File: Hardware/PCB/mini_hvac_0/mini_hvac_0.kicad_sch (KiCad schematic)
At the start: 23 parts, among them J1 Conn_01x03_Pin, J10 Conn_01x03_Pin, J11 Conn_01x03_Pin, J12 Conn_01x03_Pin, J13 Conn_01x03_Pin, J14 Conn_01x04_Pin, J15 Conn_01x04_Socket, J2 Conn_01x03_Pin, J20 Conn_01x06_Socket, J3 Conn_01x03_Pin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

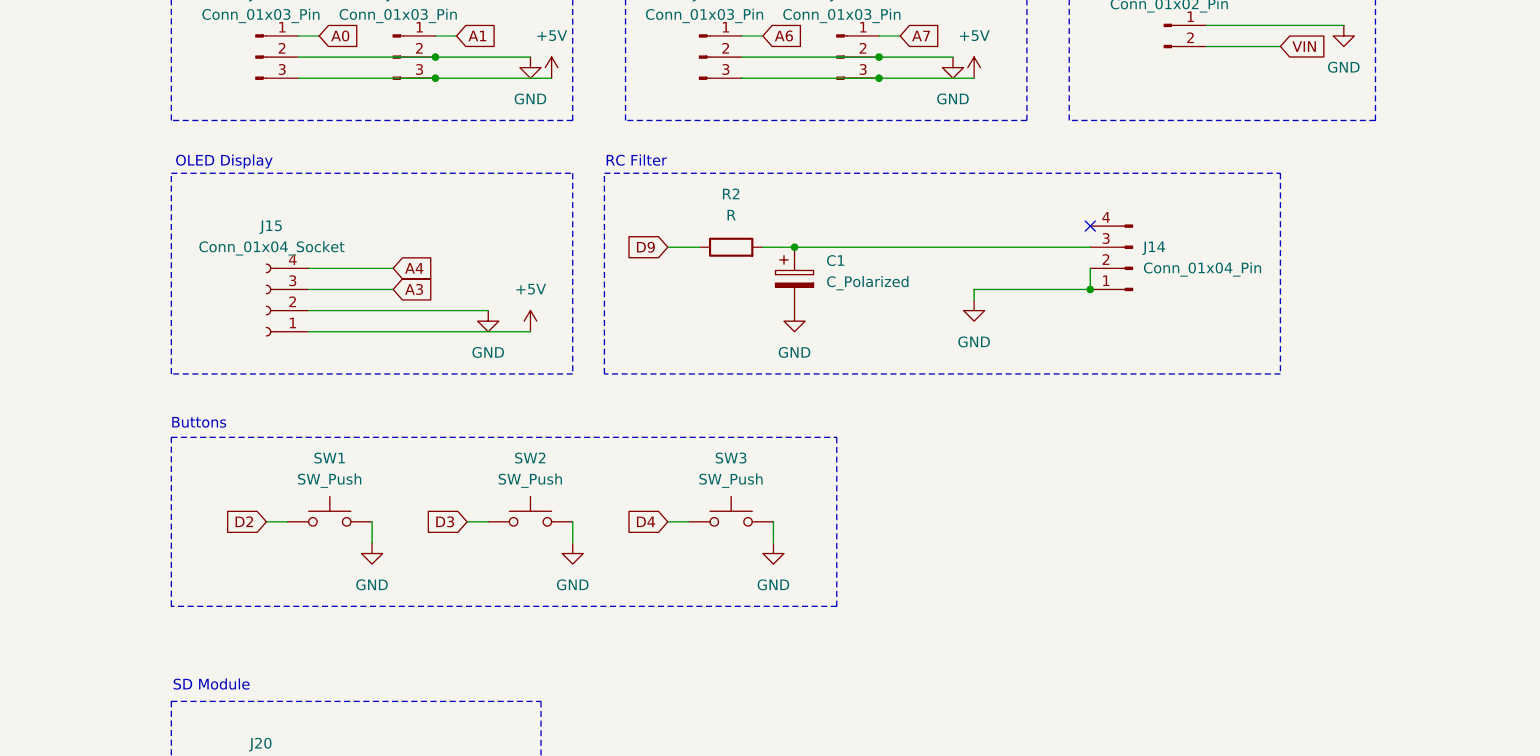
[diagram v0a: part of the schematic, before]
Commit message: added AHT header and power selector
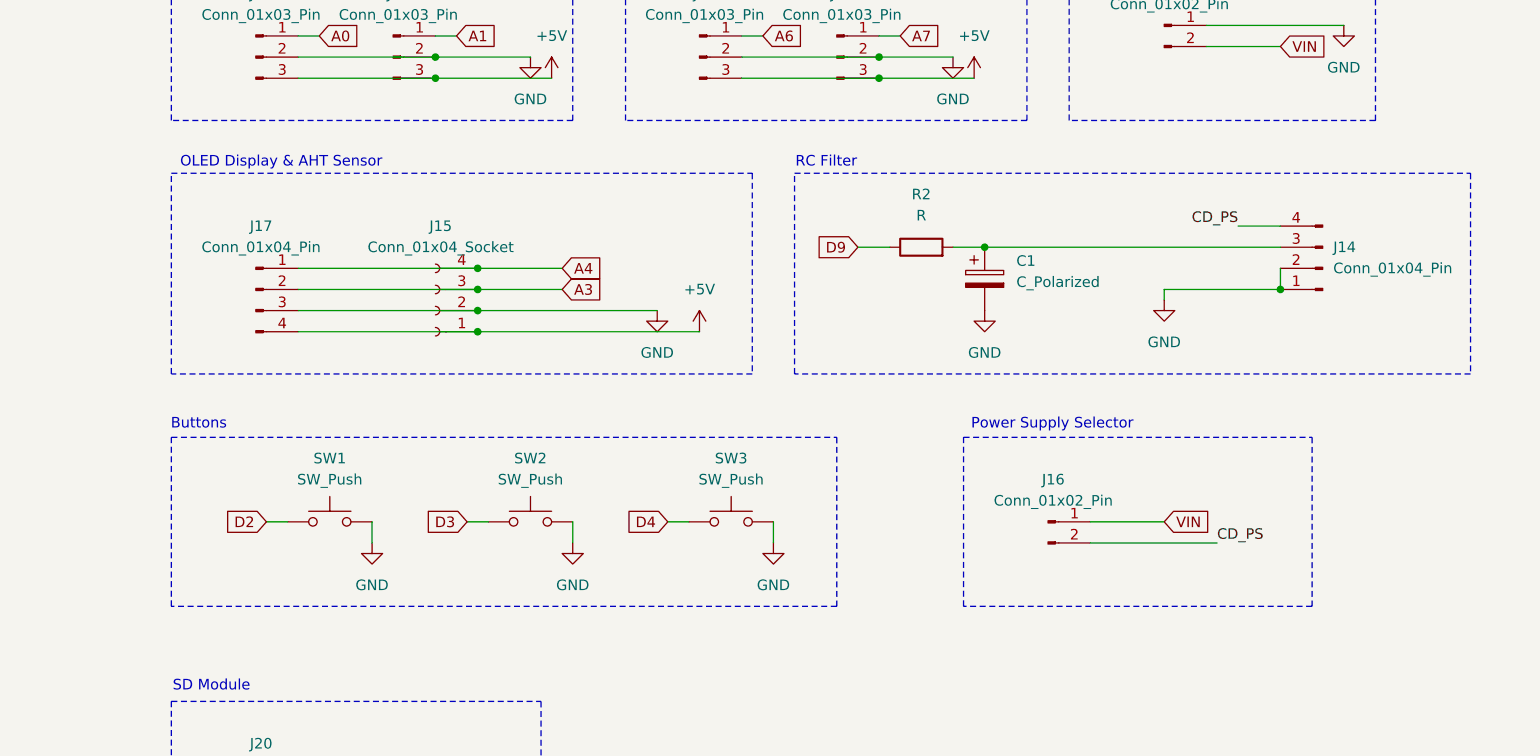
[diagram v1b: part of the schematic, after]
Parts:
- added J16: Conn_01x02_Pin, Connector_PinHeader_2.00mm:PinHeader_1x02_P2.00mm_Vertical, symbol Connector:Conn_01x02_Pin
- added J17: Conn_01x04_Pin, Connector_JST:JST_XH_B4B-XH-A_1x04_P2.50mm_Vertical, symbol Connector:Conn_01x04_Pin
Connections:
- net +5V: now also J17.4 (Pin_4)
- net A3: now also J17.2 (Pin_2)
- net A4: now also J17.1 (Pin_1)
- net GND: now also J17.3 (Pin_3)
- net VIN: now also J16.1 (Pin_1)
- net CD_PS: now reaches J14.4 (Pin_4)
- net CD_PS: now also J16.2 (Pin_2)
- no-connect marks 12 -> 11
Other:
- note added: "OLED Display & AHT Sensor"
- note added: "Power Supply Selector"
- note removed: "OLED Display"
- moved on the sheet: C1, J14, J15, R2
